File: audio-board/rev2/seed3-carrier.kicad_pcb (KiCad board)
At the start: 4 copper layers, 90 x 56.5 mm, 60 parts, among them J1 NRJ4HF, J2 SJ3-35063AG, J3 DISPLAY_UART, J4 SJ3-35063AG, J5 SPEAKER_SEND, J6 POWER_BOARD, Q1 AO3401A, Q2 2N7002, U1 TLV9061IDBVR, U2 TPA6132A2RTE

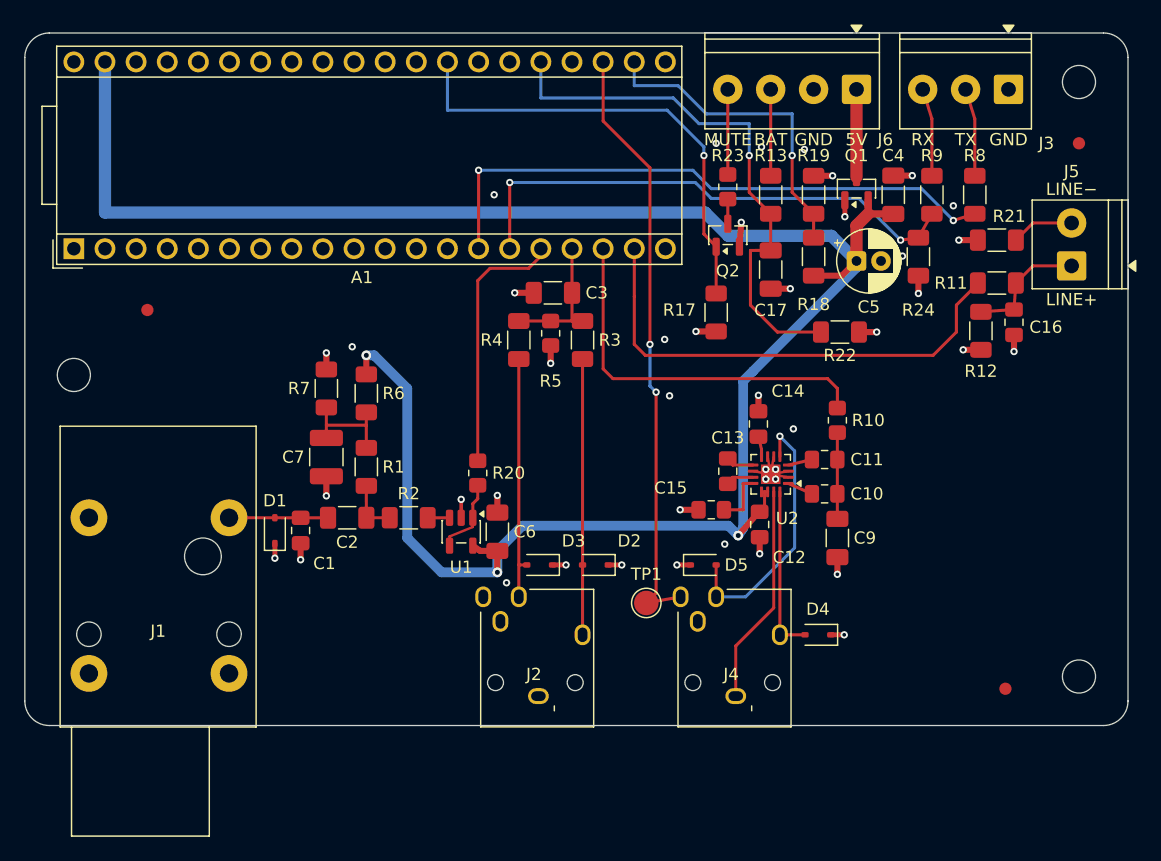
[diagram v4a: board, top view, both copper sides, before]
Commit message: Make the carrier 2-layer and hand-solderable with a MAX9722A
So the board fits a free capstone fab (2 layers, under 100 x 100 mm) and
every part can be soldered with an iron:

- U2 is now a MAX9722AEUE+ (TSSOP-16, no exposed pad) in place of the
  TPA6132A2 QFN. R25-R28 (10k 0805) set its gain to -1, for about
  0.6 Vrms full scale. C12-C15 are 1 uF, the datasheet's value. U2 and
  its parts move to the open lower-right corner, outputs straight down
  to J4.
- The stackup is 2-layer 1.6 mm, with GND pours on both sides joined by
  about 160 stitching vias. Every audio net stays on F.Cu over unbroken
  ground. Where traces cross, the non-audio one hops on B.Cu: the analog
  +5V branch, HP_DETECT and the display UART.
- The power board and UART lanes run on F.Cu between the Daisy's
  socket rows, and the Daisy's VIN runs along the rear edge.
- The circuit check gets a MAX9722A model and new test-plan readings
  for U2's charge-pump pins. DESIGN.md, CHANGES.md and TEST_PLAN.md
  describe the new amp and layout.

Board check: 0 errors, no unrouted connections, schematic parity clean.
ERC clean. Circuit check: 197 pass. Its 2 failures (guitar input under
an 18 V boost pedal) also fail on the previous commit.

Co-Authored-By: Claude Opus 5.5 <noreply@anthropic.com>
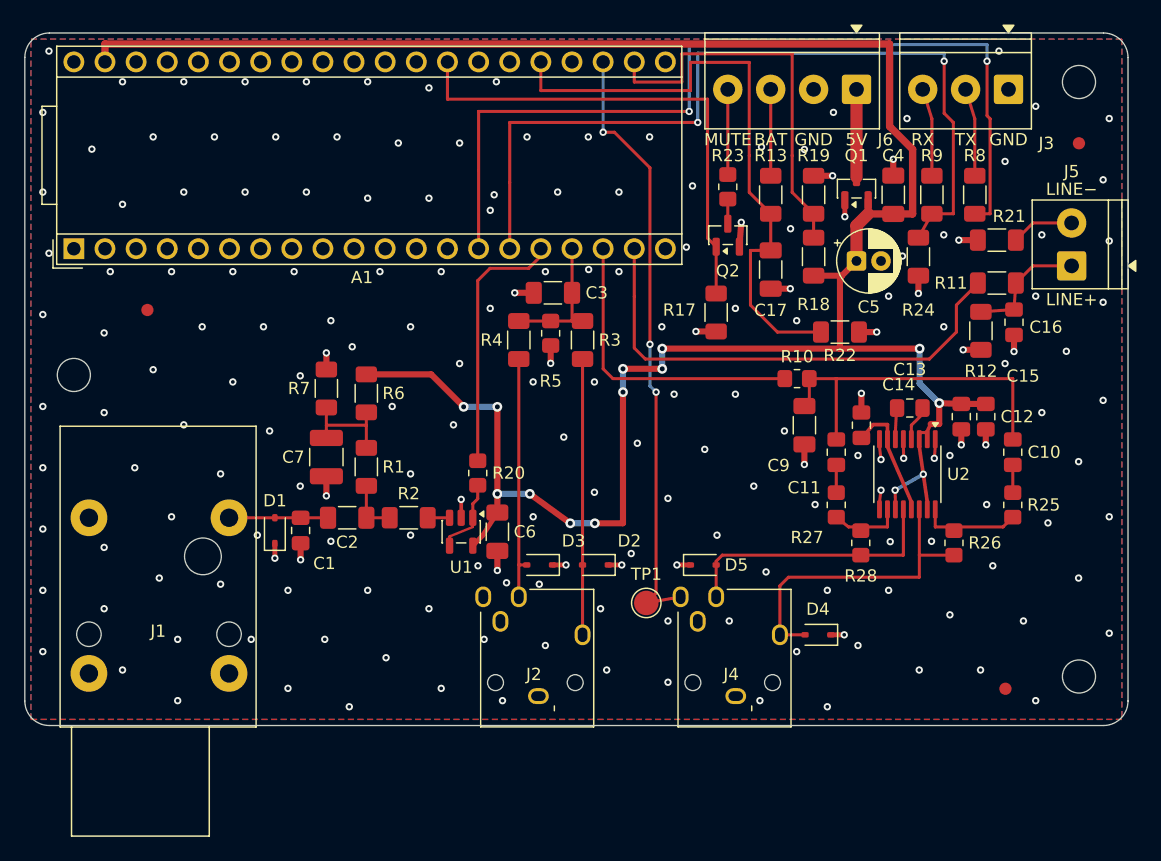
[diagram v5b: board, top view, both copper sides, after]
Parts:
- added R25: 10k, Resistor_SMD:R_0805_2012Metric_Pad1.20x1.40mm_HandSolder, F.Cu at (180.6, 88.5)
- added R26: 10k, Resistor_SMD:R_0805_2012Metric_Pad1.20x1.40mm_HandSolder, F.Cu at (175.8, 91.6)
- added R27: 10k, Resistor_SMD:R_0805_2012Metric_Pad1.20x1.40mm_HandSolder, F.Cu at (166.2, 88.5)
- added R28: 10k, Resistor_SMD:R_0805_2012Metric_Pad1.20x1.40mm_HandSolder, F.Cu at (168.2, 91.6)
- C12, C14, C15: value 2.2uF -> 1uF
- U2: value TPA6132A2RTE -> MAX9722AEUE+; footprint Package_DFN_QFN:WQFN-16-1EP_3x3mm_P0.5mm_EP1.6x1.6mm -> Package_SO:TSSOP-16_4.4x5mm_P0.65mm
- moved C15 23.7 mm to (178.4, 81.3), turned to -90 degrees
- moved C12 18.7 mm to (176.4, 81.3)
- moved C10 15.7 mm to (180.6, 84.2), turned to -90 degrees
- moved C13 15.7 mm to (172.2, 80.6), turned to 180 degrees
- moved U2 11.2 mm to (172.0, 86.0), turned to -90 degrees
- moved C9 9.59 mm to (163.6, 82.0)
- moved C14 8.40 mm to (168.2, 82.0)
- moved R10 4.73 mm to (163.0, 78.2), turned to 180 degrees
- moved C11 1.12 mm to (166.2, 84.2), turned to -90 degrees
- turned C6 to 90 degrees
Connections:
- C10 pad 2: Net-(U2-INL-) -> Net-(C10-Pad2)
- C11 pad 2: Net-(U2-INR-) -> Net-(C11-Pad2)
- C13 pad 1: Net-(U2-CPP) -> Net-(U2-C1P)
- C13 pad 2: Net-(U2-CPN) -> Net-(U2-C1N)
- C14 pad 1: Net-(U2-HPVSS) -> Net-(U2-PVSS)
- C15 pad 1: Net-(U2-HPVDD) -> +5V
- U2 pad 1: Net-(U2-INL-) -> GND
- U2 pad 10: GND -> Net-(U2-INR-)
- U2 pad 11: Net-(U2-CPP) -> +5V
- U2 pad 12: Net-(U2-HPVDD) -> /HP_R
- U2 pad 13: +5V -> Net-(U2-PVSS)
- U2 pad 14: +5V -> /HP_L
- U2 pad 15: GND -> +5V
- U2 pad 16: /HP_L -> Net-(U2-INL-)
- U2 pad 2: GND -> +5V
- U2 pad 3: GND -> +5V
- U2 pad 4: Net-(U2-INR-) -> Net-(U2-C1P)
- U2 pad 5: /HP_R -> GND
- U2 pad 6: GND -> Net-(U2-C1N)
- U2 pad 7: GND -> Net-(U2-PVSS)
- U2 pad 8: Net-(U2-HPVSS) -> GND
- U2 pad 9: Net-(U2-CPN) -> GND
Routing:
- net /DISPLAY_UART_RX: track 42.9 -> 68.8 mm
- net /DISPLAY_UART_TX: track 48.7 -> 73.3 mm
- net +5V: track 170.3 -> 193.1 mm, vias 3 -> 14
- net /HP_SOURCE: track 7.04 -> 28.5 mm
- net GND: track 60.3 -> 42.4 mm, vias 43 -> 194
- net /HP_L: track 13.7 -> 25.2 mm
- net Net-(U2-PVSS): track 0.00 -> 7.59 mm
- net /AUDIO_OUT_1: track 31.2 -> 25.0 mm
- net /5V_SENSE: track 26.6 -> 32.5 mm, vias 1 -> 0
- net /BATT_SENSE: track 44.6 -> 50.5 mm, vias 1 -> 0
- net Net-(U2-INL-): track 2.10 -> 7.46 mm
- net Net-(U2-HPVDD): track 4.53 -> 0.00 mm
- net Net-(U2-INR-): track 1.98 -> 5.26 mm
- net Net-(U2-CPP): track 2.33 -> 0.00 mm
- net Net-(U2-CPN): track 2.33 -> 0.00 mm
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- added copper zone on B.Cu, net GND
- added copper zone on F.Cu, net GND
- removed copper zone on In1.Cu, net GND
- removed copper zone on In2.Cu, net GND
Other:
- copper layers 4 -> 2
